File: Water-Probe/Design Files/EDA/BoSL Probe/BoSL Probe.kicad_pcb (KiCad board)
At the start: 2 copper layers, 29 x 18 mm, 8 parts, among them J1 8P8C_Shielded, J2 Screw_Terminal_01x03, U1 MS5803-01BA, U2 DS18B20

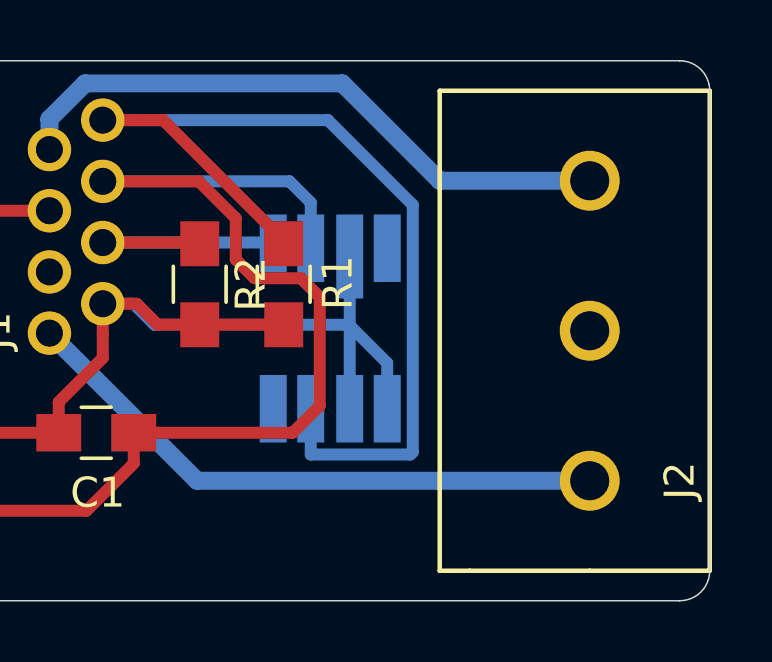
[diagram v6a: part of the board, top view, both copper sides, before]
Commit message: transmit code added to gps
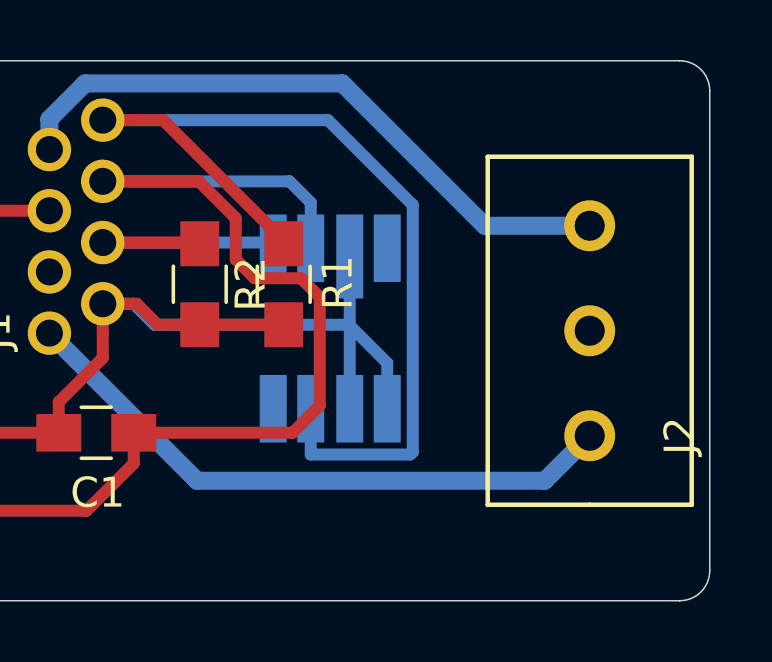
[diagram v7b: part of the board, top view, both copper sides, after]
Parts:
- J2: footprint Project:Screw_Terminals_1x3 -> Project:Screw_Terminals_1x3_3.5mm
- moved J2 1.50 mm to (125.0, 103.5)
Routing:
- net A3: track 20.9 -> 21.5 mm
- net A0: track 20.0 -> 20.7 mm
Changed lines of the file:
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@@
     )
   )
-  (module Project:Screw_Terminals_1x3 (layer F.Cu)
-    (at 125 105 90)
+  (module Project:Screw_Terminals_1x3_3.5mm (layer F.Cu)
+    (at 125 103.5 90)
     (fp_text reference J2 (at 0 3 90) (layer F.SilkS)
       (effects (font (size 1 1) (thickness 0.15)))
     )
-    (fp_text value Screw_Terminal_01x03 (at 5 -3 90) (layer F.Fab)
+    (fp_text value Screw_Terminal_01x03 (at 8.3 -4.4 90) (layer F.Fab)
       (effects (font (size 1 1) (thickness 0.15)))
     )
-    (fp_line (start -3 -5) (end -3 -4) (layer F.SilkS) (width 0.15))
-    (fp_line (start 13 -5) (end -3 -5) (layer F.SilkS) (width 0.15))
-    (fp_line (start -3 0) (end -3 4) (layer F.SilkS) (width 0.15))
-    (fp_line (start -3 4) (end 13 4) (layer F.SilkS) (width 0.15))
-    (fp_line (start -3 -4) (end -3 0) (layer F.SilkS) (width 0.15))
-    (fp_line (start 13 -5) (end 13 4) (layer F.SilkS) (width 0.15))
-    (pad 3 thru_hole circle (at 10 0 90) (size 2 2) (drill 1.3) (layers *.Cu *.Mask)
+    (fp_line (start -2.3 0) (end -2.3 3.4) (layer F.SilkS) (width 0.15))
+    (fp_line (start -2.3 3.4) (end 9.3 3.4) (layer F.SilkS) (width 0.15))
+    (fp_line (start 9.3 3.4) (end 9.3 -3.4) (layer F.SilkS) (width 0.15))
+    (fp_line (start 9.3 -3.4) (end -2.3 -3.4) (layer F.SilkS) (width 0.15))
+    (fp_line (start -2.3 -3.4) (end -2.3 0) (layer F.SilkS) (width 0.15))
+    (pad 3 thru_hole circle (at 7 0 90) (size 1.7 1.7) (drill 1) (layers *.Cu *.Mask)
       (net 4 A3))
-    (pad 2 thru_hole circle (at 5 0 90) (size 2 2) (drill 1.3) (layers *.Cu *.Mask))
-    (pad 1 thru_hole circle (at 0 0 90) (size 2 2) (drill 1.3) (layers *.Cu *.Mask)
+    (pad 1 thru_hole circle (at 0 0 90) (size 1.7 1.7) (drill 1) (layers *.Cu *.Mask)
       (net 3 A0))
+    (pad 2 thru_hole circle (at 3.5 0 90) (size 1.7 1.7) (drill 1) (layers *.Cu *.Mask))
   )
   (gr_text "BoSL-Probe\nrev 0.2" (at 114 107) (layer B.SilkS)
@@
   (segment (start 103.2 100.2) (end 103.2 103.26) (width 0.4) (layer F.Cu) (net 2) (status 30))
   (segment (start 114.8 99.8) (end 112 99.8) (width 0.4) (layer F.Cu) (net 2) (status 30))
-  (segment (start 119.96 105) (end 125 105) (width 0.6) (layer B.Cu) (net 3))
-  (segment (start 106.99 100.08) (end 111.91 105) (width 0.6) (layer B.Cu) (net 3))
-  (segment (start 111.91 105) (end 119.96 105) (width 0.6) (layer B.Cu) (net 3))
+  (segment (start 106.99 100.08) (end 111.91 105) (width 0.6) (layer B.Cu) (net 3) (status 10))
+  (segment (start 123.5 105) (end 111.91 105) (width 0.6) (layer B.Cu) (net 3))
+  (segment (start 125 103.5) (end 123.5 105) (width 0.6) (layer B.Cu) (net 3))
+  (segment (start 121.5 96.5) (end 125 96.5) (width 0.6) (layer B.Cu) (net 4))
+  (segment (start 116.754999 91.754999) (end 121.5 96.5) (width 0.6) (layer B.Cu) (net 4))
+  (segment (start 108.179999 91.754999) (end 116.754999 91.754999) (width 0.6) (layer B.Cu) (net 4))
+  (segment (start 106.99 93.96) (end 106.99 92.944998) (width 0.6) (layer B.Cu) (net 4))
   (segment (start 106.99 92.944998) (end 108.179999 91.754999) (width 0.6) (layer B.Cu) (net 4))
-  (segment (start 106.99 93.96) (end 106.99 92.944998) (width 0.6) (layer B.Cu) (net 4) (status 10))
-  (segment (start 108.179999 91.754999) (end 116.754999 91.754999) (width 0.6) (layer B.Cu) (net 4))
-  (segment (start 120 95) (end 125 95) (width 0.6) (layer B.Cu) (net 4))
-  (segment (start 116.754999 91.754999) (end 120 95) (width 0.6) (layer B.Cu) (net 4))
   (segment (start 114.26 97.06) (end 114.45 97.25) (width 0.4) (layer B.Cu) (net 5) (status 30))
   (segment (start 108.768 97.06) (end 114.26 97.06) (width 0.4) (layer B.Cu) (net 5) (status 30))
